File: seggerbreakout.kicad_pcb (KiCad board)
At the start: 2 copper layers, 2 parts, among them P1 SWD, P2 JTAG

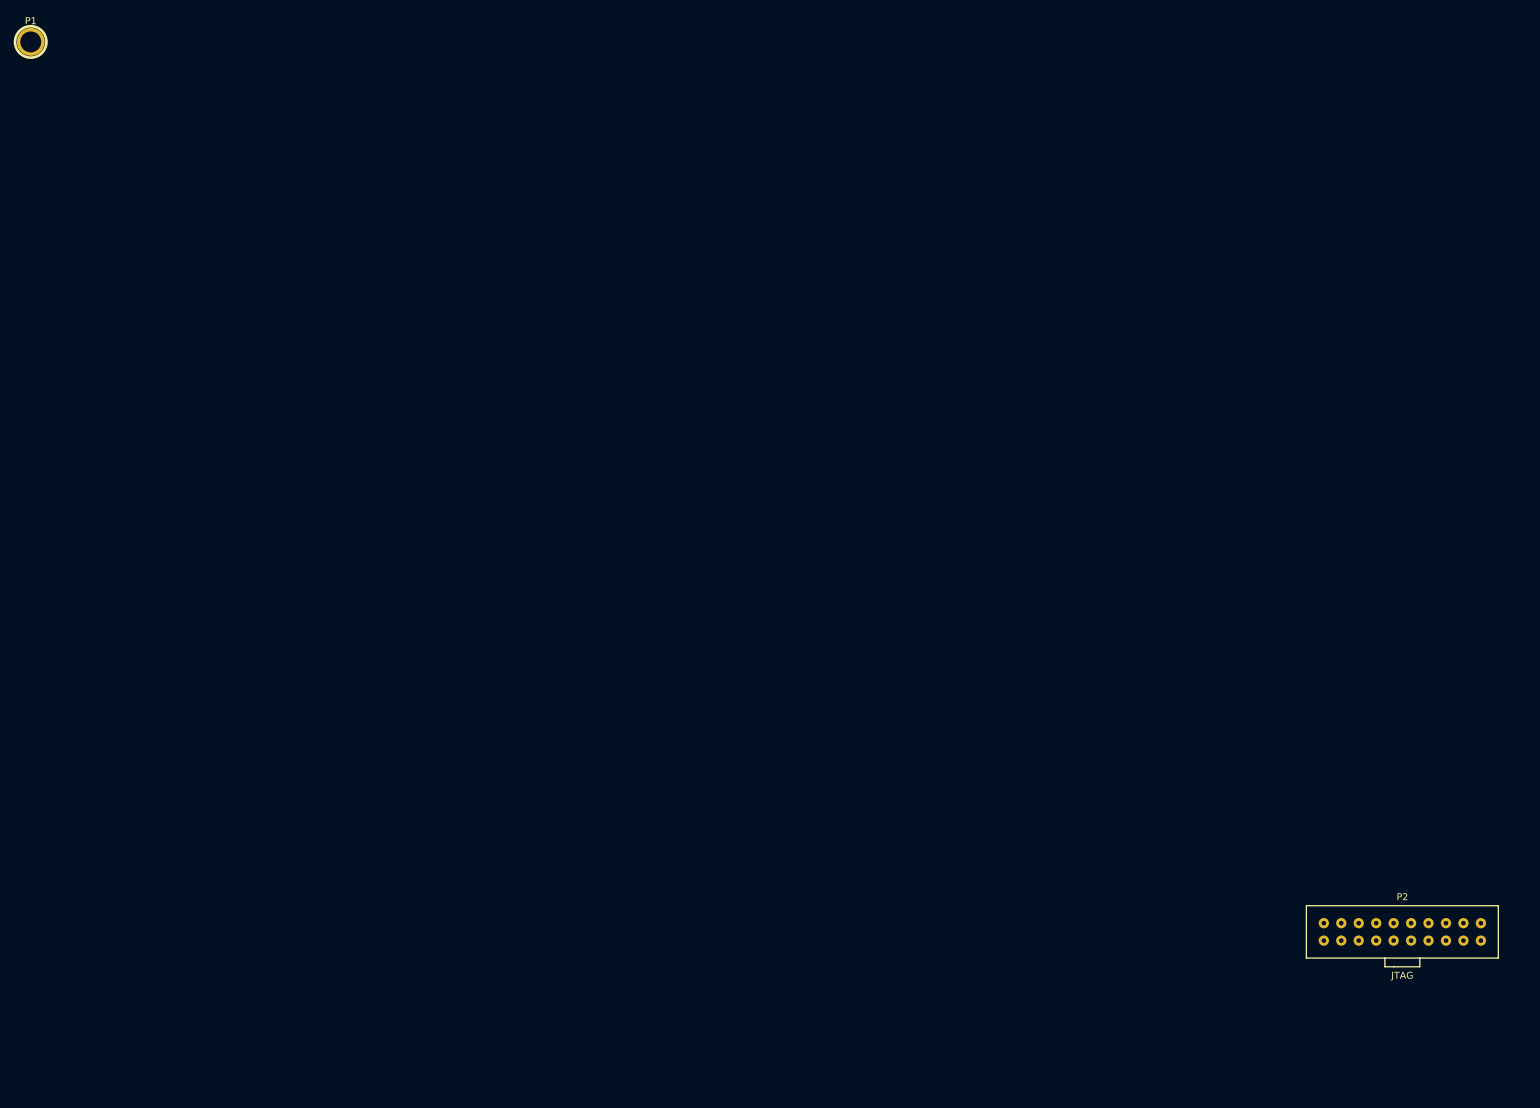
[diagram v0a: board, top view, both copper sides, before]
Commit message: add swd and 2x5 swd connector
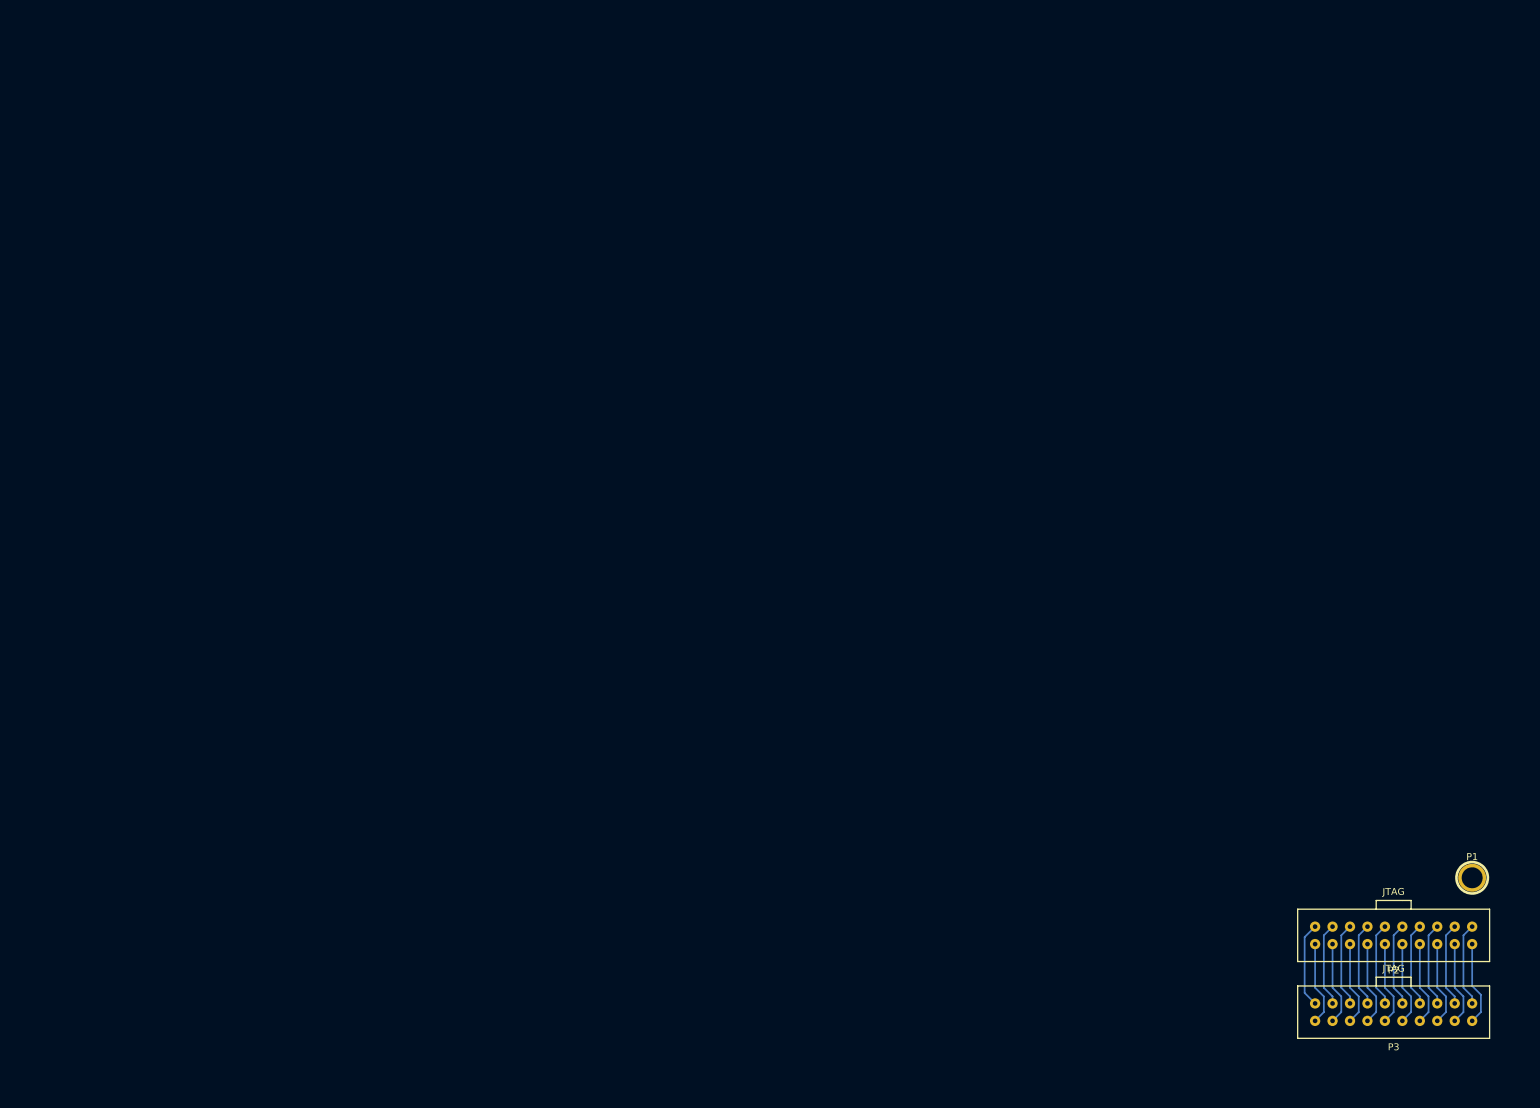
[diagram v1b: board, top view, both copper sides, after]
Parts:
- added P3: JTAG, SEGGER_INPUT, F.Cu at (198.4, 140.0)
- moved P1 242.5 mm to (209.8, 121.7)
- moved P2 2.40 mm to (198.4, 128.8), turned to 180 degrees
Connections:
- P2 pad 2: (no net) -> N-000008
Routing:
- net N-0000018: track 0.00 -> 12.4 mm
- net N-0000021: track 0.00 -> 12.2 mm
- net N-0000019: track 0.00 -> 12.2 mm
- net N-0000017: track 0.00 -> 12.2 mm
- net N-0000016: track 0.00 -> 12.2 mm
- net N-0000014: track 0.00 -> 12.2 mm
- net N-0000013: track 0.00 -> 12.2 mm
- net N-000001: track 0.00 -> 12.2 mm
- net N-000006: track 0.00 -> 12.2 mm
- net N-000005: track 0.00 -> 12.2 mm
- net N-000002: track 0.00 -> 12.2 mm
- net N-0000015: track 0.00 -> 12.2 mm
- net N-0000010: track 0.00 -> 12.2 mm
- net N-000008: track 0.00 -> 12.2 mm
- net N-0000012: track 0.00 -> 12.2 mm
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
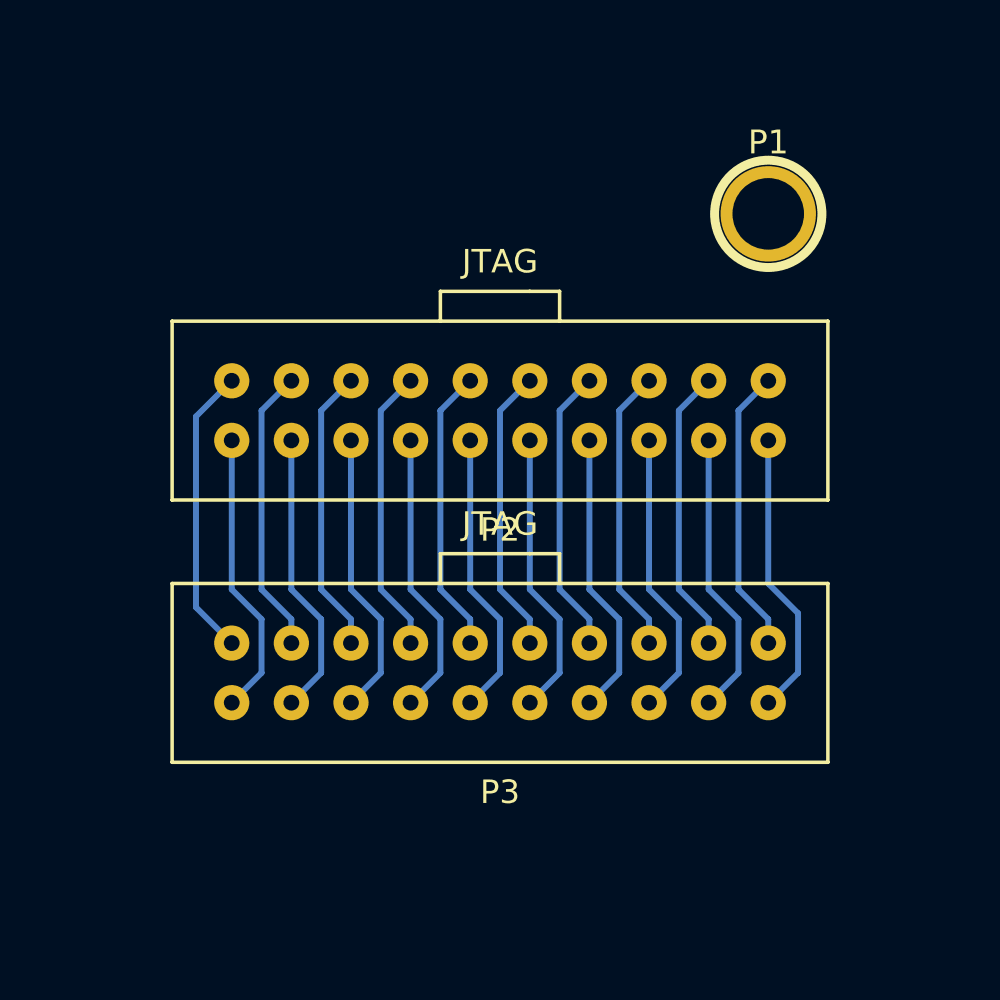
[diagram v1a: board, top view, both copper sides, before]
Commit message: Sent out for fabrication
Vendor: OSHPark, LLC
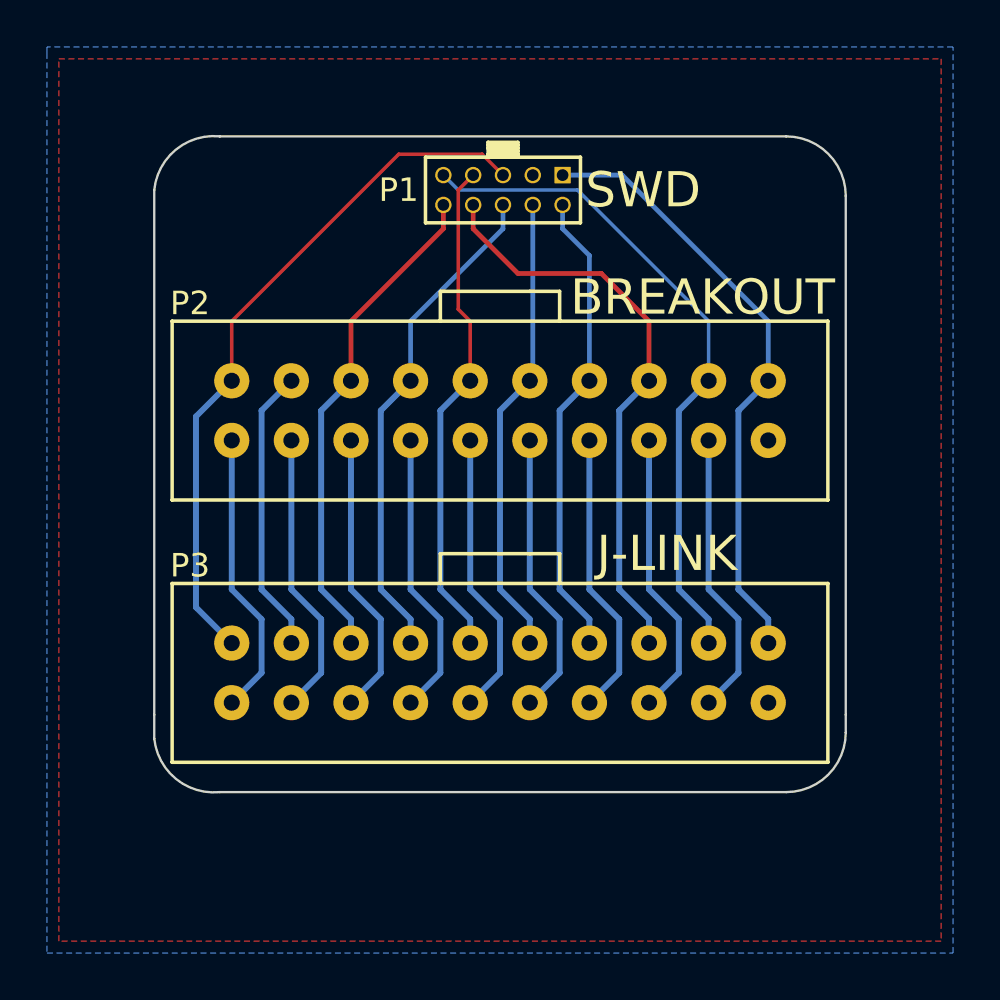
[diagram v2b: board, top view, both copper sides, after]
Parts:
- P1: footprint 1pin -> JTAG_SMALL
- moved P1 10.7 mm to (199.1, 120.7)
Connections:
- net N-0000017 renamed /DBGRQ
- net N-0000019 renamed /VTref
- P2 pad 10: N-000004 -> GND
- P2 pad 11: N-000001 -> /RTCK
- P2 pad 12: N-000003 -> GND
- P2 pad 13: N-0000011 -> /TDO
- P2 pad 14: N-000006 -> GND
- P2 pad 15: N-0000021 -> /RESET
- P2 pad 16: N-0000010 -> GND
- P2 pad 18: N-000009 -> GND
- P2 pad 19: N-0000018 -> /5V
- P2 pad 2: N-000008 -> (no net)
- P2 pad 20: N-0000015 -> GND
- P2 pad 3: N-0000016 -> /nTRST
- P2 pad 4: N-000007 -> GND
- P2 pad 5: N-0000012 -> /TDI
- P2 pad 6: N-000002 -> GND
- P2 pad 7: N-0000013 -> /TMS
- P2 pad 8: N-000005 -> GND
- P2 pad 9: N-0000014 -> /TCK
- P3 pad 10: N-000004 -> GND
- P3 pad 11: N-000001 -> /RTCK
- P3 pad 12: N-000003 -> GND
- P3 pad 13: N-0000011 -> /TDO
- P3 pad 14: N-000006 -> GND
- P3 pad 15: N-0000021 -> /RESET
- P3 pad 16: N-0000010 -> GND
- P3 pad 18: N-000009 -> GND
- P3 pad 19: N-0000018 -> /5V
- P3 pad 2: N-000008 -> (no net)
- P3 pad 20: N-0000015 -> GND
- P3 pad 3: N-0000016 -> /nTRST
- P3 pad 4: N-000007 -> GND
- P3 pad 5: N-0000012 -> /TDI
- P3 pad 6: N-000002 -> GND
- P3 pad 7: N-0000013 -> /TMS
- P3 pad 8: N-000005 -> GND
- P3 pad 9: N-0000014 -> /TCK
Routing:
- net GND: track 0.00 -> 110.1 mm
- net /5V: track 0.00 -> 29.8 mm
- net /nTRST: track 0.00 -> 28.6 mm
- net /TDI: track 0.00 -> 24.9 mm
- net /RTCK: track 0.00 -> 21.5 mm
- net /RESET: track 0.00 -> 21.4 mm
- net /TDO: track 0.00 -> 21.4 mm
- net /TMS: track 0.00 -> 20.2 mm
- net /TCK: track 0.00 -> 19.8 mm
- net /VTref: track 12.2 -> 26.1 mm
- net N-0000018: track 12.4 -> 0.00 mm
- net N-0000021: track 12.2 -> 0.00 mm
- net N-0000016: track 12.2 -> 0.00 mm
- net N-0000014: track 12.2 -> 0.00 mm
- net N-0000013: track 12.2 -> 0.00 mm
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- added copper zone on B.Cu, net GND
- added copper zone on F.Cu, net GND
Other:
- board outline added: 29.5 x 28 mm
- net class Min added: clearance 0.1524, trace_width 0.1524, via_dia 0.508, via_drill 0.3302
- net class SWD added: clearance 0.1524, trace_width 0.1524, via_dia 0.889, via_drill 0.635
- rule trace_min: 0.254 -> 0.1524
- rule via_min_drill: 0.508 -> 0.3302
- rule via_min_size: 0.889 -> 0.508
- board text added: "5V DBGRQ RESET TDO RTCK TCK TMS TDI nTRST VTref"
- board text added: "BREAKOUT"
- board text added: "GND"
- board text added: "J-LINK"
- board text added: "J-LINK Breakout+SWD 2014-08-18 open.konspyre.org/jswd"
- board text added: "SWD"

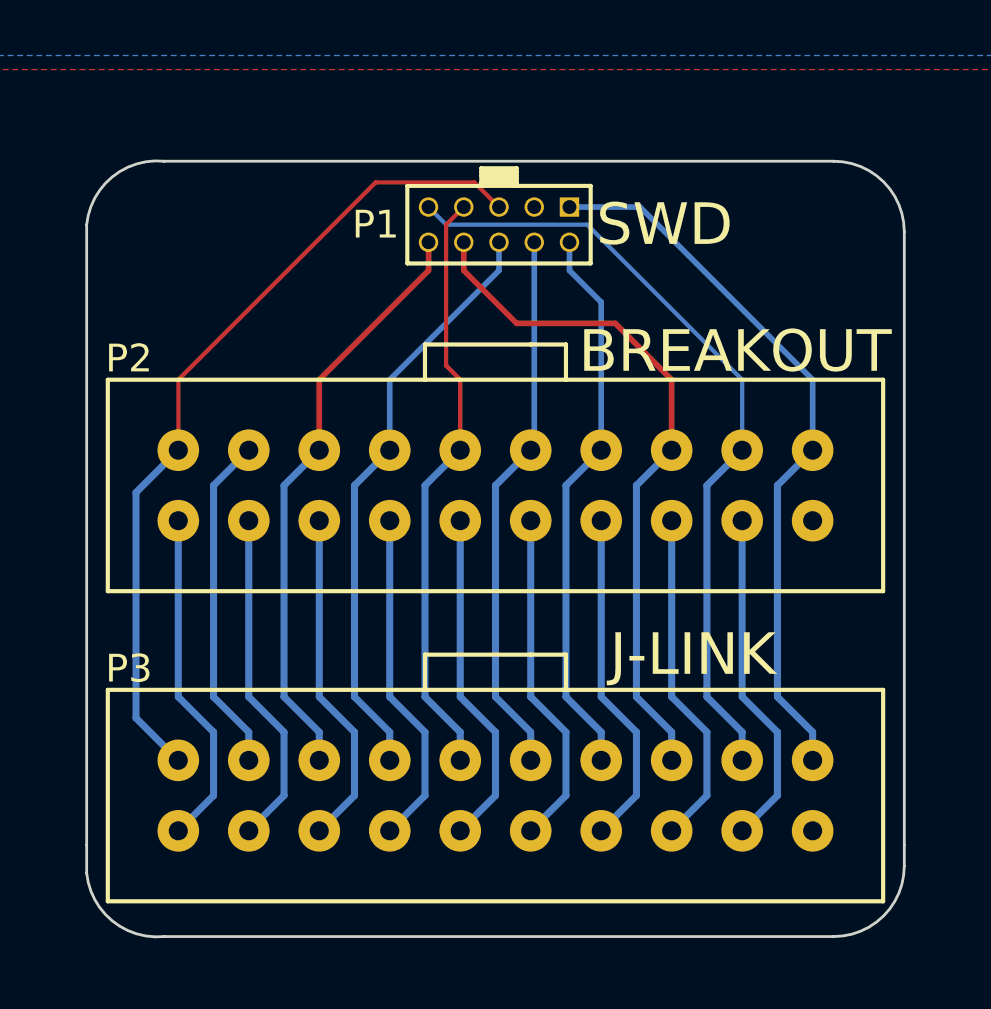
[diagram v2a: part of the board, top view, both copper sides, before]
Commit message: fix hole sizes!
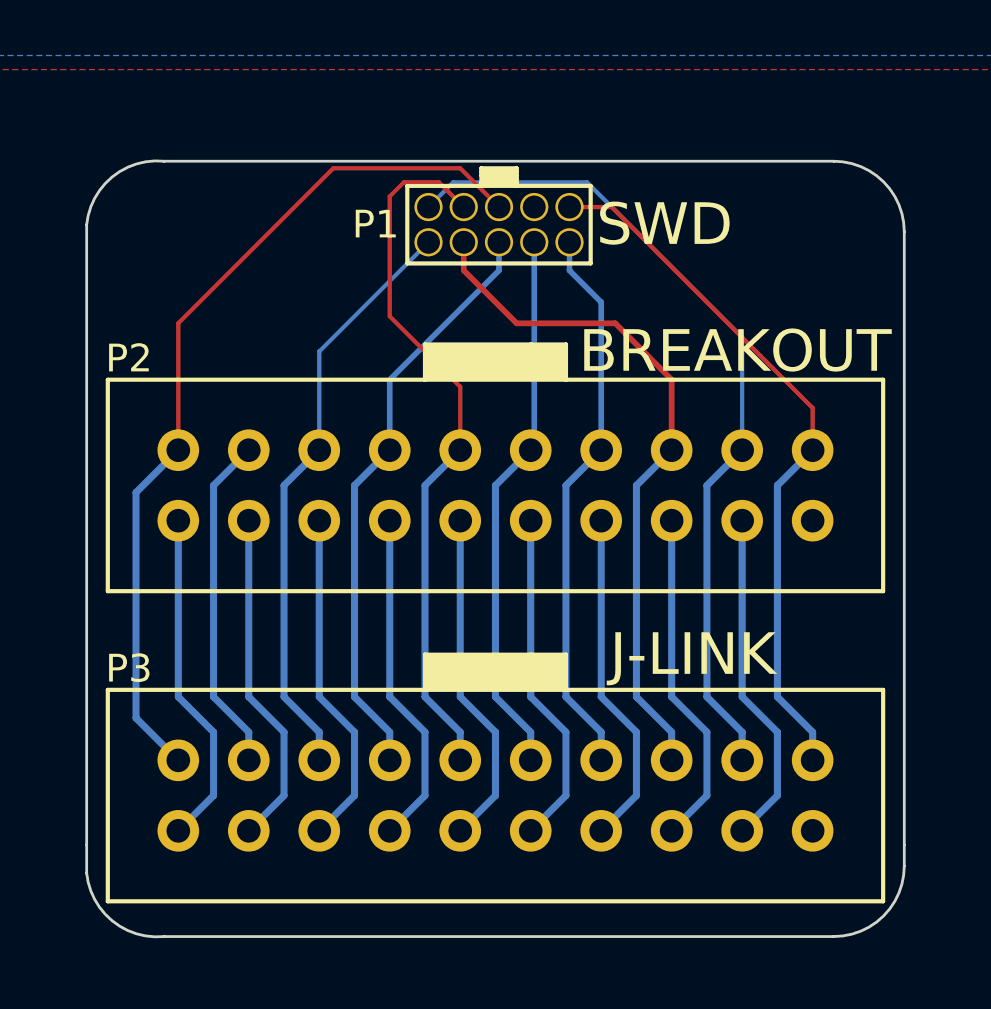
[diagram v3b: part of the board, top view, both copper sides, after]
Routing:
- net /RTCK: track 21.5 -> 25.7 mm
- net /nTRST: track 28.6 -> 30.3 mm
- net /5V: track 29.8 -> 31.5 mm
- net /VTref: track 26.1 -> 25.5 mm
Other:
- net class Default: clearance 0.254 -> 0.1524
- rule trace_clearance: 0.254 -> 0.1524
